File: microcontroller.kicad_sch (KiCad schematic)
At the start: 40 parts, among them J4 Conn_01x02, J5 SWD, SW1 SW_SPDT, U2 STM32F105RCTx, U3 SN65HVD230, U4 CD143A-SR05, Y1 16MHz

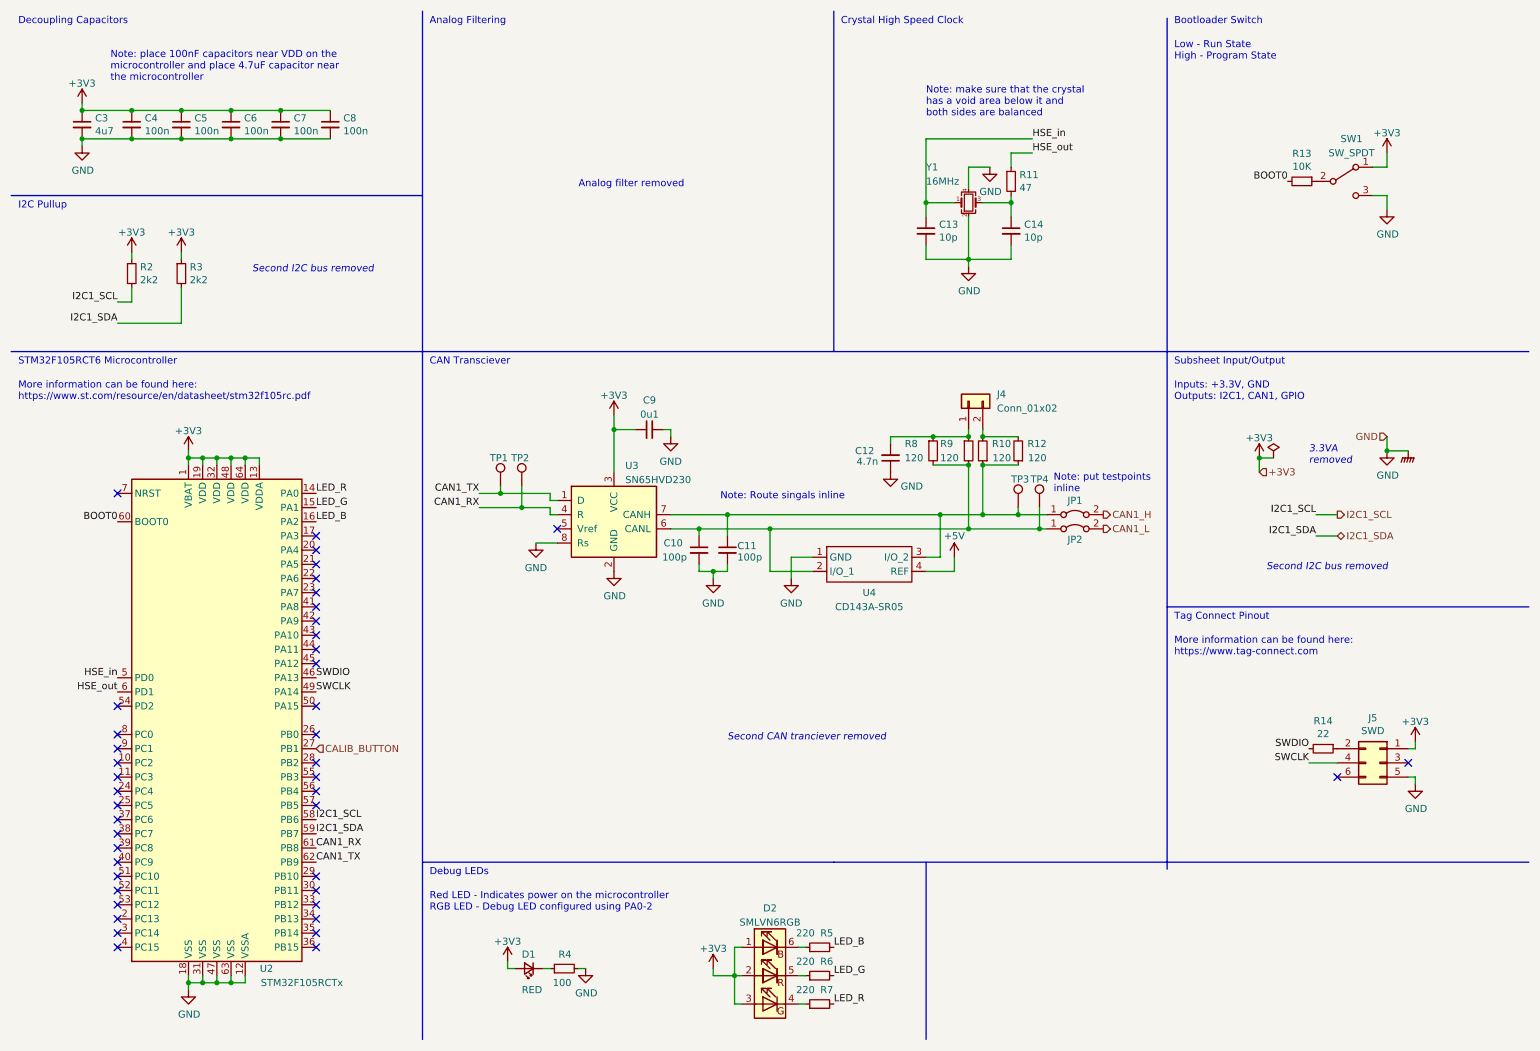
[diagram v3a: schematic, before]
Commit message: Added 0 Ω resistor to shield, grounded it, reannotated schematic, reassigned some footprints
Starting layout
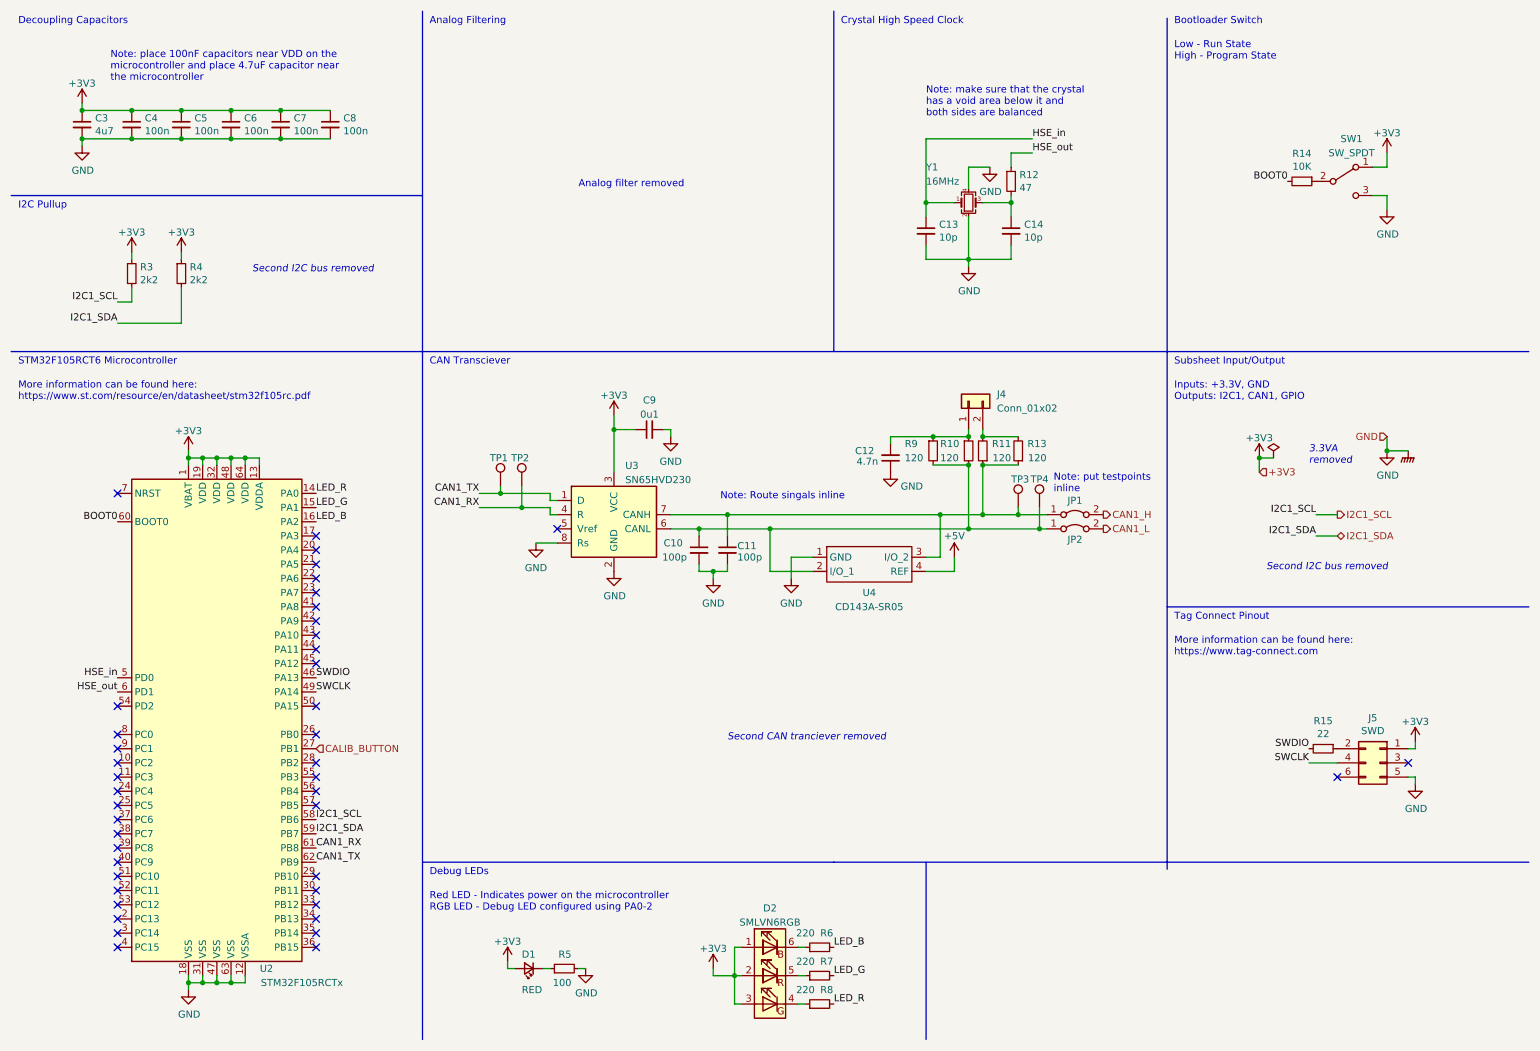
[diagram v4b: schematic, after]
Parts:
- C10, C11, C12, C13, C14, C3, C4, C5, C6, C7, C8, C9: footprint Capacitor_SMD:C_0603_1608Metric -> Capacitor_SMD:C_0603_1608Metric_Pad1.08x0.95mm_HandSolder
- D1: footprint LED_SMD:LED_0603_1608Metric -> LED_SMD:LED_0603_1608Metric_Pad1.05x0.95mm_HandSolder
- R10: renamed from R9; footprint Resistor_SMD:R_0603_1608Metric -> Resistor_SMD:R_0603_1608Metric_Pad0.98x0.95mm_HandSolder
- R11: renamed from R10; footprint Resistor_SMD:R_0603_1608Metric -> Resistor_SMD:R_0603_1608Metric_Pad0.98x0.95mm_HandSolder
- R12: renamed from R11; footprint Resistor_SMD:R_0603_1608Metric -> Resistor_SMD:R_0603_1608Metric_Pad0.98x0.95mm_HandSolder
- R13: renamed from R12; footprint Resistor_SMD:R_0603_1608Metric -> Resistor_SMD:R_0603_1608Metric_Pad0.98x0.95mm_HandSolder
- R14: renamed from R13; footprint Resistor_SMD:R_0603_1608Metric -> Resistor_SMD:R_0603_1608Metric_Pad0.98x0.95mm_HandSolder
- R15: renamed from R14; footprint Resistor_SMD:R_0603_1608Metric -> Resistor_SMD:R_0603_1608Metric_Pad0.98x0.95mm_HandSolder
- R3: renamed from R2; footprint Resistor_SMD:R_0603_1608Metric -> Resistor_SMD:R_0603_1608Metric_Pad0.98x0.95mm_HandSolder
- R4: renamed from R3; footprint Resistor_SMD:R_0603_1608Metric -> Resistor_SMD:R_0603_1608Metric_Pad0.98x0.95mm_HandSolder
- R5: renamed from R4; footprint Resistor_SMD:R_0603_1608Metric -> Resistor_SMD:R_0603_1608Metric_Pad0.98x0.95mm_HandSolder
- R6: renamed from R5; footprint Resistor_SMD:R_0603_1608Metric -> Resistor_SMD:R_0603_1608Metric_Pad0.98x0.95mm_HandSolder
- R7: renamed from R6; footprint Resistor_SMD:R_0603_1608Metric -> Resistor_SMD:R_0603_1608Metric_Pad0.98x0.95mm_HandSolder
- R8: renamed from R7; footprint Resistor_SMD:R_0603_1608Metric -> Resistor_SMD:R_0603_1608Metric_Pad0.98x0.95mm_HandSolder
- R9: renamed from R8; footprint Resistor_SMD:R_0603_1608Metric -> Resistor_SMD:R_0603_1608Metric_Pad0.98x0.95mm_HandSolder

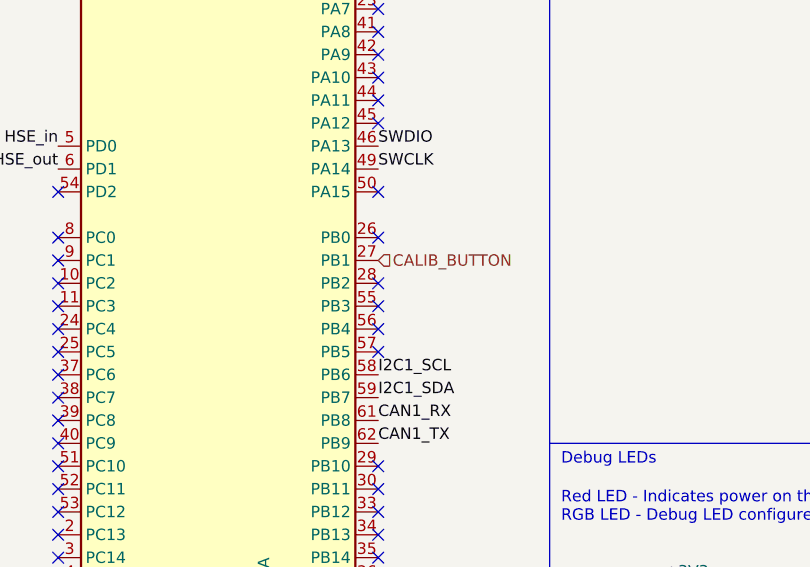
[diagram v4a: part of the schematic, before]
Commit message: Added EEPROM chip for storing calibration data
Time to redo layout
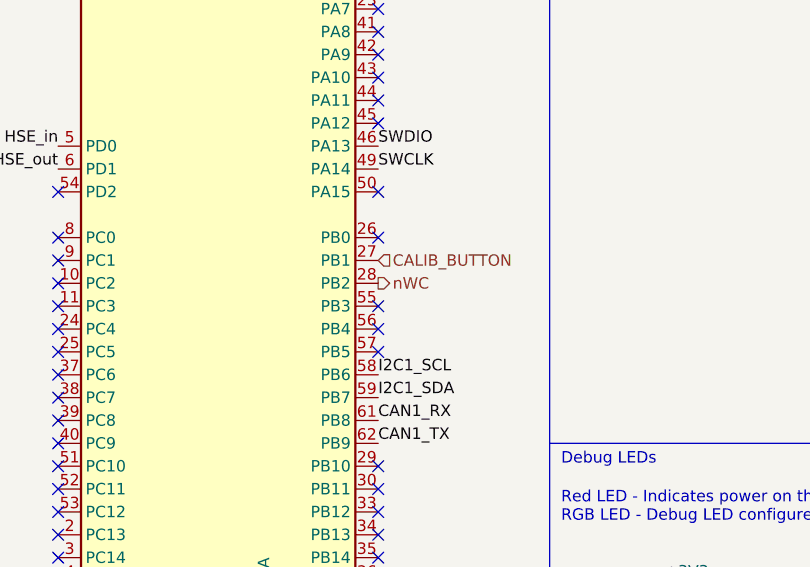
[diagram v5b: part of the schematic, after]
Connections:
- net nWC: now reaches U2.28 (PB2)
- no-connect marks 43 -> 42
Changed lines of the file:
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@@
   (no_connect (at 67.31 175.26))
   (no_connect (at 67.31 172.72))
-  (no_connect (at 67.31 147.32))
   (no_connect (at 67.31 127))
   (no_connect (at 67.31 129.54))
@@
     (effects (font (size 1.27 1.27)) (justify left))
   )
+  (hierarchical_label "nWC" (shape output) (at 67.31 147.32 0)
+    (effects (font (size 1.27 1.27)) (justify left))
+  )
